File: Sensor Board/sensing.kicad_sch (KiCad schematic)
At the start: 10 parts, among them J2 Irradience Sensor, J5 CAN Bus Connector, U5 INA180

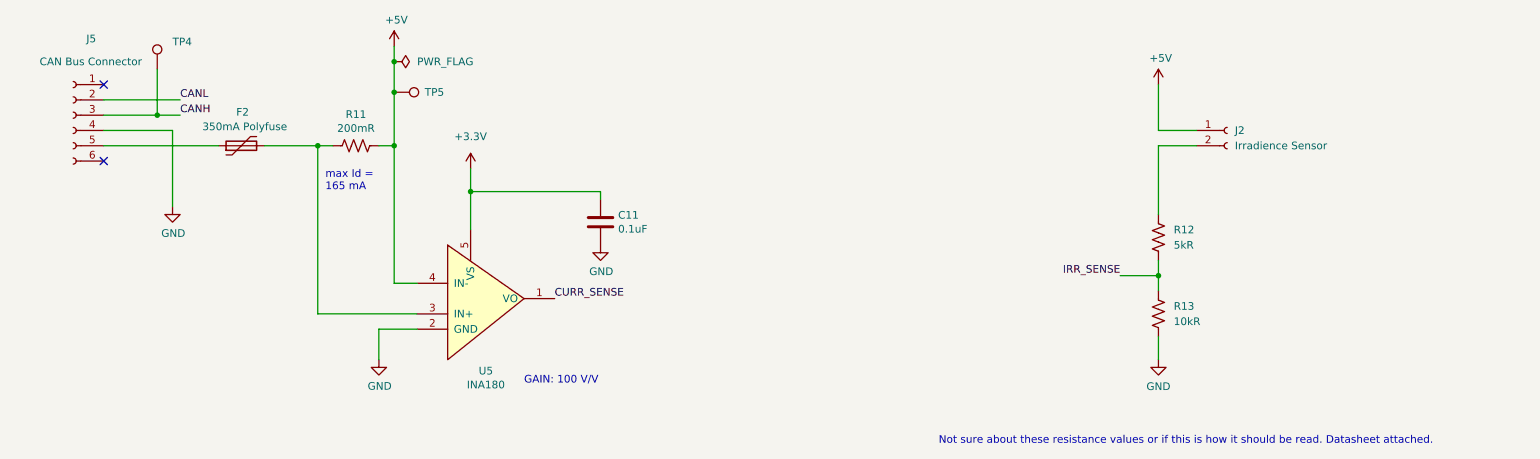
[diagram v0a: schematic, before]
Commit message: Finish schematics and footprint assignments
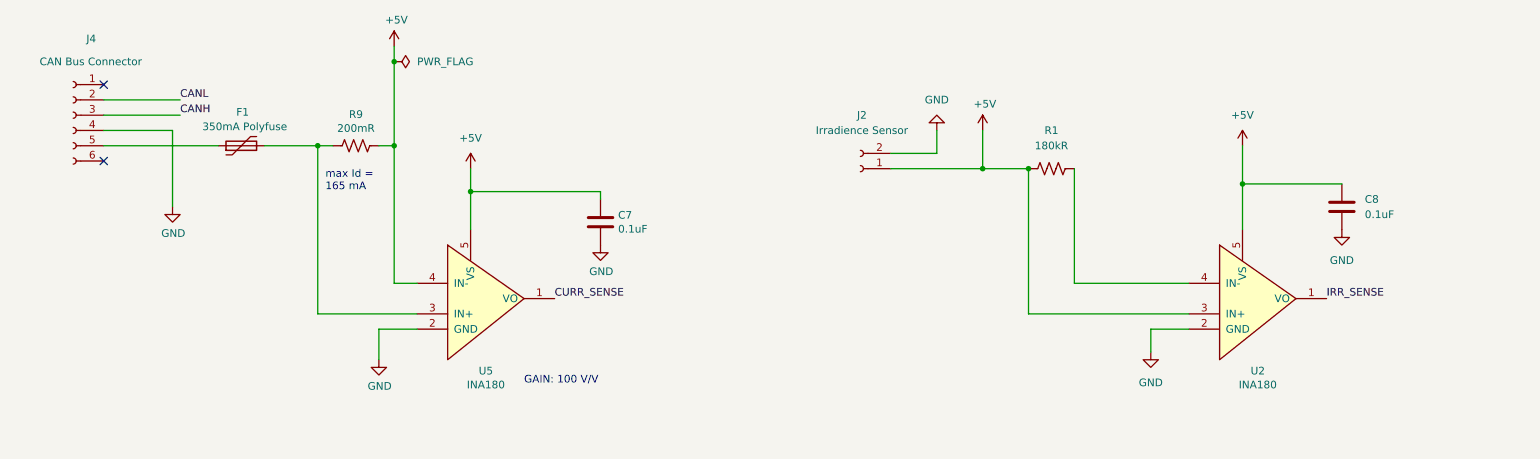
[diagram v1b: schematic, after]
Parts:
- removed R12: 5kR, Resistor_SMD:R_0805_2012Metric_Pad1.20x1.40mm_HandSolder, symbol Device:R_US
- removed R13: 10kR, Resistor_SMD:R_0805_2012Metric_Pad1.20x1.40mm_HandSolder, symbol Device:R_US
- removed TP4, TP5: ~, TestPoint:TestPoint_Pad_1.0x1.0mm, symbol canhw:TestPointDefault
- added C8: 0.1uF, Capacitor_SMD:C_0805_2012Metric_Pad1.18x1.45mm_HandSolder, symbol Device:C
- added R1: 180kR, Resistor_SMD:R_0805_2012Metric_Pad1.20x1.40mm_HandSolder, symbol Device:R_US
- added U2: INA180, Package_TO_SOT_SMD:SOT-23-5_HandSoldering, symbol canhw:INA180
- J2: footprint (none) -> Canhw:P16612-011CA
- J4: renamed from J5; footprint canhw:connector_Harwin_G125–MG10605M4P -> Canhw:connector_Harwin_G125–MG10605M4P
- renumbered C11 to C7, F2 to F1, R11 to R9
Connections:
- net +3.3V is gone; now on net +5V: C7.1, U5.5 (VS)
- net +5V: now also C8.1, R1.1, U2.3 (IN+), U2.5 (VS)
- net GND: now also J2.2 (Pin_2), C8.2, U2.2 (GND)
- net IRR_SENSE: now also U2.1 (VO)
- new net: R1.2, U2.4 (IN-)
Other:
- note removed: "Not sure about these resistance values or if this is how it should be read. Datasheet attached."
- moved on the sheet: J2

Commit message: fix labels
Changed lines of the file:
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@@
+	(wire
+		(pts
+			(xy 62.23 49.53) (xy 45.72 49.53)
+		)
+		(stroke
+			(width 0)
+			(type default)
+		)
+	)
 	(wire
 		(pts
@@
 	(wire
 		(pts
-			(xy 45.72 49.53) (xy 58.42 49.53)
-		)
-		(stroke
-			(width 0)
-			(type default)
-		)
-	)
-	(wire
-		(pts
 			(xy 234.95 60.96) (xy 234.95 54.61)
 		)
@@
 	(wire
 		(pts
-			(xy 58.42 46.99) (xy 45.72 46.99)
-		)
-		(stroke
-			(width 0)
-			(type default)
-		)
-	)
-	(wire
-		(pts
 			(xy 93.98 77.47) (xy 93.98 54.61)
 		)
@@
 	(wire
 		(pts
+			(xy 62.23 44.45) (xy 62.23 49.53)
+		)
+		(stroke
+			(width 0)
+			(type default)
+		)
+	)
+	(wire
+		(pts
 			(xy 45.72 52.07) (xy 57.15 52.07)
 		)
@@
 	(wire
 		(pts
+			(xy 57.15 44.45) (xy 57.15 46.99)
+		)
+		(stroke
+			(width 0)
+			(type default)
+		)
+	)
+	(wire
+		(pts
 			(xy 72.39 54.61) (xy 81.28 54.61)
+		)
+		(stroke
+			(width 0)
+			(type default)
+		)
+	)
+	(wire
+		(pts
+			(xy 57.15 46.99) (xy 45.72 46.99)
 		)
 		(stroke
@@
 		)
 	)
-	(label "CANH"
-		(at 58.42 49.53 0)
+	(global_label "CANL"
+		(shape input)
+		(at 57.15 44.45 90)
 		(fields_autoplaced yes)
 		(effects
@@
 				(size 1.27 1.27)
 			)
-			(justify left bottom)
-		)
-	)
-	(label "CURR_SENSE"
+			(justify left)
+		)
+		(property "Intersheetrefs" "${INTERSHEET_REFS}"
+			(at 57.15 36.7476 90)
+			(effects
+				(font
+					(size 1.27 1.27)
+				)
+				(justify left)
+				(hide yes)
+			)
+		)
+	)
+	(global_label "CANH"
+		(shape input)
+		(at 62.23 44.45 90)
+		(fields_autoplaced yes)
+		(effects
+			(font
+				(size 1.27 1.27)
+			)
+			(justify left)
+		)
+		(property "Intersheetrefs" "${INTERSHEET_REFS}"
+			(at 62.23 36.4452 90)
+			(effects
+				(font
+					(size 1.27 1.27)
+				)
+				(justify left)
+				(hide yes)
+			)
+		)
+	)
+	(global_label "CURR_SENSE"
+		(shape input)
 		(at 120.65 80.01 0)
 		(fields_autoplaced yes)
@@
 				(size 1.27 1.27)
 			)
-			(justify left bottom)
-		)
-	)
-	(label "CANL"
-		(at 58.42 46.99 0)
-		(fields_autoplaced yes)
-		(effects
-			(font
-				(size 1.27 1.27)
-			)
-			(justify left bottom)
-		)
-	)
-	(label "IRR_SENSE"
+			(justify left)
+		)
+		(property "Intersheetrefs" "${INTERSHEET_REFS}"
+			(at 135.7908 80.01 0)
+			(effects
+				(font
+					(size 1.27 1.27)
+				)
+				(justify left)
+				(hide yes)
+			)
+		)
+	)
+	(global_label "IRR_SENSE"
+		(shape input)
 		(at 248.92 80.01 0)
 		(fields_autoplaced yes)
@@
 				(size 1.27 1.27)
 			)
-			(justify left bottom)
-		)
-	)
+			(justify left)
+		)
+		(property "Intersheetrefs" "${INTERSHEET_REFS}"
+			(at 262.0651 80.01 0)
+			(effects
+				(font
+					(size 1.27 1.27)
+				)
+				(justify left)
+				(hide yes)
+			)
+		)
+	)

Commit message: Fix comments from review
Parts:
- R1: value 180kR -> 1MR
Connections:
- net +5V: no longer J2.1 (Pin_1), R1.1, U2.3 (IN+)
- net GND: now also J2.1 (Pin_1); no longer J2.2 (Pin_2)
- new net: J2.2 (Pin_2), R1.1, U2.3 (IN+)
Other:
- note added: "Datasheet on this 'connector' is for sensor"
- note added: "Expected incident light should result in photocurrent of ~10nA-1uA, so 5v = (1uA)*R gives resistance ~5MR"
- moved on the sheet: C8, R1, U2
